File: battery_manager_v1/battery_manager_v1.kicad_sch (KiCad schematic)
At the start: 1 part

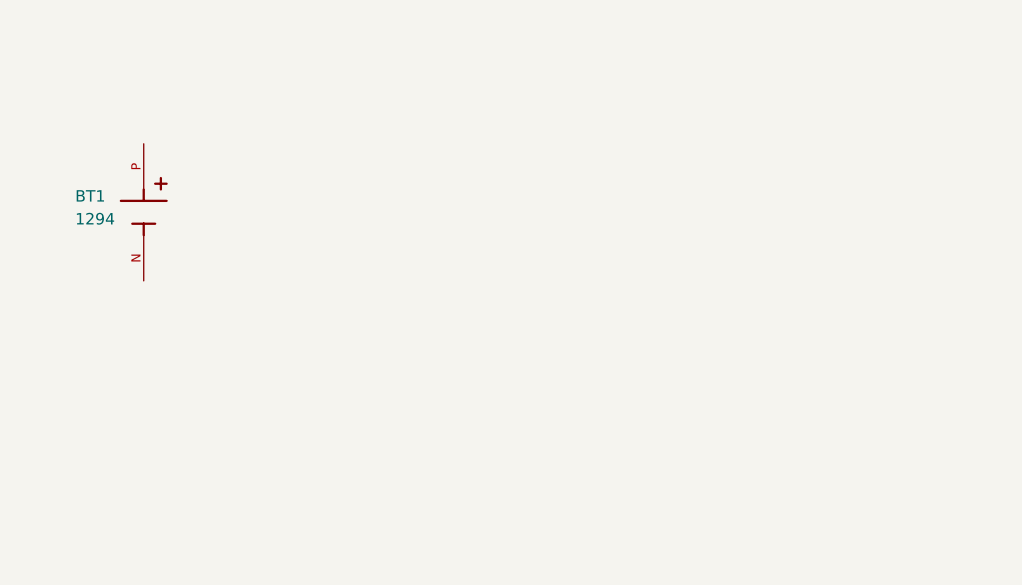
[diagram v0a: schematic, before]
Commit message: Added Regulators etc.
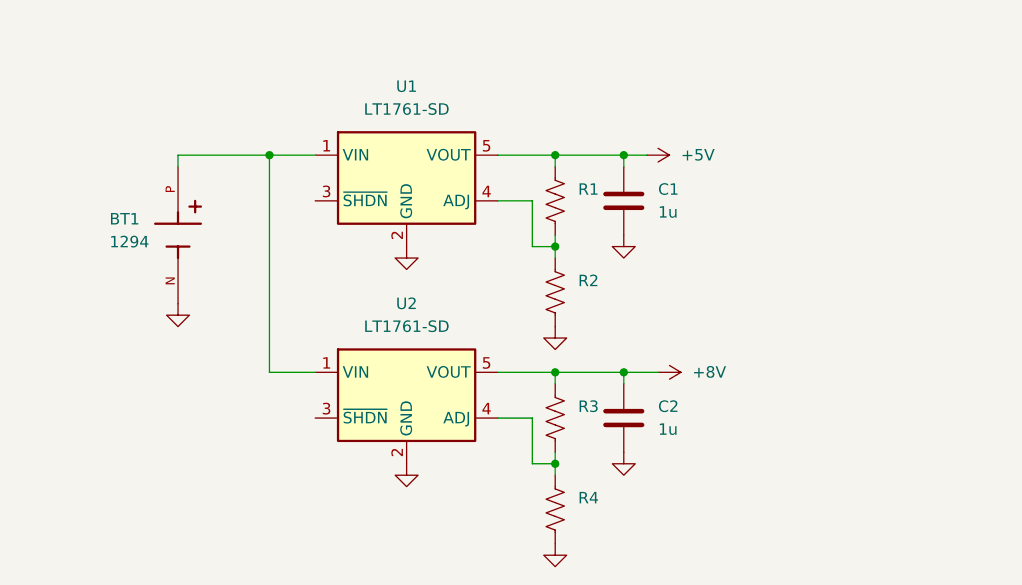
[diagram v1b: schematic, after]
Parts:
- added C1, C2: 1u, Capacitor_SMD:C_0603_1608Metric, symbol Device:C
- added R1, R2, R3, R4: R_US, Resistor_SMD:R_0603_1608Metric, symbol Device:R_US
- added U1, U2: LT1761-SD, Package_TO_SOT_SMD:TSOT-23-5, symbol Regulator_Linear:LT1761-SD
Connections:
- net GND: now reaches BT1.N
- net GND: now also C1.2, C2.2, R2.2, R4.2, U1.2 (GND), U2.2 (GND)
- net at BT1.P: now also U1.1 (VIN), U2.1 (VIN)
- new net: R1.2, R2.1, U1.4 (ADJ)
- new net: R3.2, R4.1, U2.4 (ADJ)
- new net +5V: C1.1, R1.1, U1.5 (VOUT)
- new net +8V: C2.1, R3.1, U2.5 (VOUT)
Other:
- moved on the sheet: BT1

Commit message: V1 Final Before Update to V2
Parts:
- added H1, H2, H3: MountingHole_Pad, MountingHole:MountingHole_3.2mm_M3_DIN965_Pad_TopOnly, symbol Mechanical:MountingHole_Pad
- added J1, J2: Conn_01x02, Connector_JST:JST_PH_S2B-PH-K_1x02_P2.00mm_Horizontal, symbol Connector_Generic:Conn_01x02
- added SW1: SS-12F44-G5, LCSC Parts:SW-TH_SS-12F44-G5, symbol LCSC Symbols:SS-12F44-G5
- BT1: footprint Battery Holder (Horizontal):BAT_1294 -> LCSC Parts:BAT_1294
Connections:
- net +5V: now also J2.1 (Pin_1)
- net +8V: now also J1.1 (Pin_1)
- net GND: now also H1.1, H2.1, H3.1, J1.2 (Pin_2), J2.2 (Pin_2), SW1.3, SW1.4, SW1.5
- net at U1.1 (VIN), U2.1 (VIN): now also SW1.2; no longer BT1.P
- new net: BT1.P, SW1.1
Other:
- moved on the sheet: BT1

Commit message: Updates and first creation of gerbers
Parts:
- removed H3: MountingHole_Pad, MountingHole:MountingHole_3.2mm_M3_DIN965_Pad_TopOnly, symbol Mechanical:MountingHole_Pad
- R1: value R_US -> 40k
- R2, R4: value R_US -> 10k
- R3: value R_US -> 68k
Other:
- moved on the sheet: J2
